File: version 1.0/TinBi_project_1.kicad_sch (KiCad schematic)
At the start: 57 parts

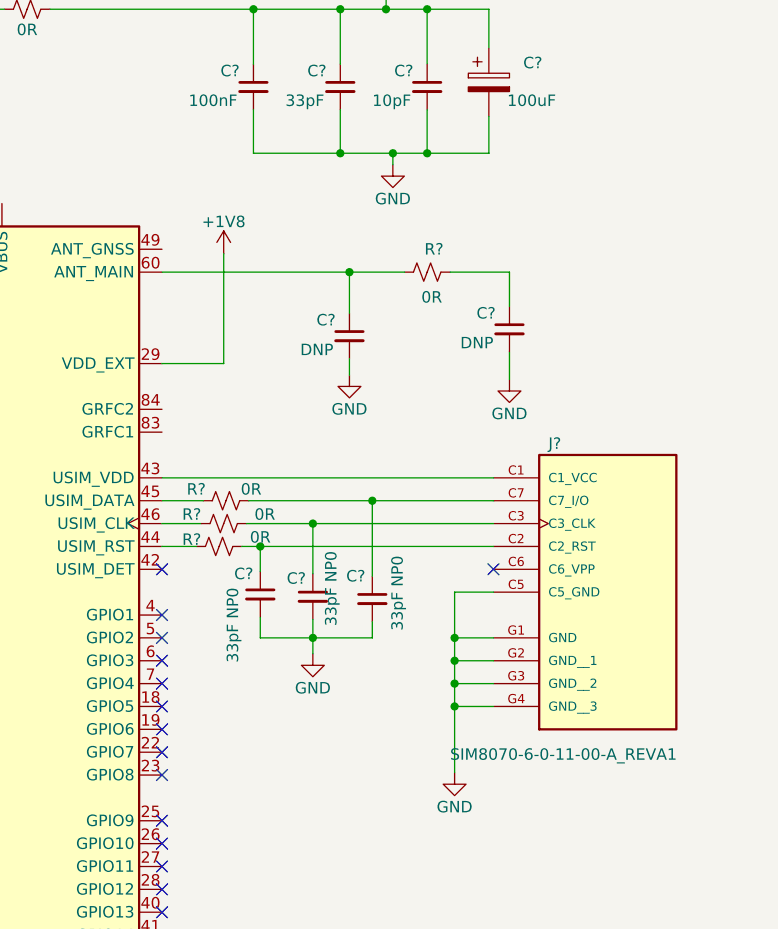
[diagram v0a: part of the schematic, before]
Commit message: Updated with the antenna symbols and library
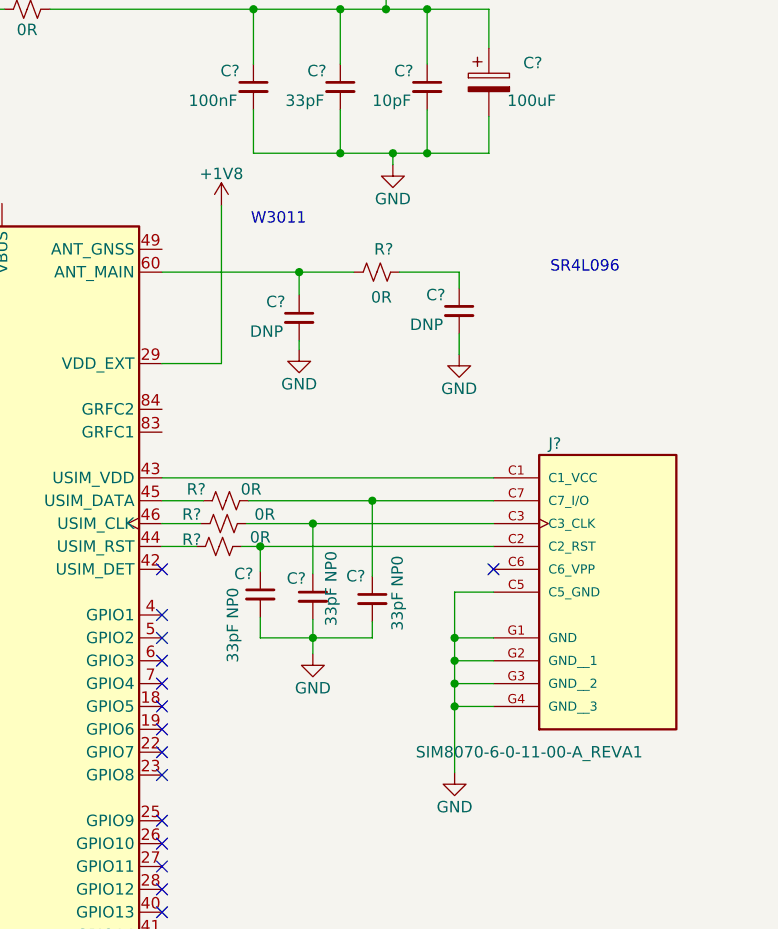
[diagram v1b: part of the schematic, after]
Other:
- note added: "SR4L096"
- note added: "W3011"
- moved on the sheet: C?, R?
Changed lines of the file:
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@@
 		)
 	)
+	(text "SR4L096 "
+		(exclude_from_sim no)
+		(at 371.094 61.976 0)
+		(effects
+			(font
+				(size 1.27 1.27)
+			)
+		)
+	)
 	(text "RESET CIRCUITRY"
 		(exclude_from_sim no)
@@
 		)
 	)
+	(text "W3011 "
+		(exclude_from_sim no)
+		(at 337.058 56.642 0)
+		(effects
+			(font
+				(size 1.27 1.27)
+			)
+		)
+	)
 	(text "Place close as possible \nto the individual VDD pins"
 		(exclude_from_sim no)
@@
 	)
 	(junction
-		(at 344.932 62.484)
+		(at 339.344 62.484)
 		(diameter 0)
 		(color 0 0 0 0)
@@
 	(wire
 		(pts
-			(xy 351.028 62.484) (xy 344.932 62.484)
+			(xy 345.44 62.484) (xy 339.344 62.484)
 		)
 		(stroke
@@
 	(wire
 		(pts
-			(xy 330.962 60.452) (xy 330.962 72.644)
+			(xy 330.708 55.118) (xy 330.708 72.644)
 		)
 		(stroke
@@
 	(wire
 		(pts
-			(xy 356.108 62.484) (xy 362.712 62.484)
+			(xy 350.52 62.484) (xy 357.124 62.484)
 		)
 		(stroke
@@
 	(wire
 		(pts
-			(xy 344.932 62.484) (xy 344.932 67.056)
+			(xy 339.344 62.484) (xy 339.344 65.024)
 		)
 		(stroke
@@
 	(wire
 		(pts
-			(xy 344.932 73.914) (xy 344.932 72.136)
+			(xy 339.344 71.12) (xy 339.344 70.104)
 		)
 		(stroke
@@
 	(wire
 		(pts
-			(xy 324.104 62.484) (xy 344.932 62.484)
+			(xy 324.104 62.484) (xy 339.344 62.484)
 		)
 		(stroke
@@
 	(wire
 		(pts
-			(xy 362.712 74.422) (xy 362.712 71.374)
+			(xy 357.124 71.628) (xy 357.124 69.342)
 		)
 		(stroke
@@
 	(wire
 		(pts
-			(xy 362.712 62.484) (xy 362.712 66.294)
+			(xy 357.124 62.484) (xy 357.124 64.262)
 		)
 		(stroke
@@
 	(wire
 		(pts
-			(xy 324.104 72.644) (xy 330.962 72.644)
+			(xy 324.104 72.644) (xy 330.708 72.644)
 		)
 		(stroke
@@
 		)
 		(property "Value" "SIM8070-6-0-11-00-A_REVA1"
-			(at 356.108 116.078 0)
+			(at 352.298 115.824 0)
 			(effects
 				(font
@@
 	(symbol
 		(lib_id "PCM_SparkFun-PowerSymbol:GND")
-		(at 362.712 74.422 0)
+		(at 357.124 71.628 0)
 		(unit 1)
 		(exclude_from_sim no)
@@
 		(fields_autoplaced yes)
 		(property "Reference" "#PWR042"
-			(at 362.712 80.772 0)
+			(at 357.124 77.978 0)
 			(effects
 				(font
@@
 		)
 		(property "Value" "GND"
-			(at 362.712 78.232 0)
+			(at 357.124 75.438 0)
 			(do_not_autoplace yes)
 			(effects
@@
 		)
 		(property "Footprint" ""
-			(at 362.712 74.422 0)
+			(at 357.124 71.628 0)
 			(effects
 				(font
@@
 		)
 		(property "Datasheet" ""
-			(at 362.712 74.422 0)
+			(at 357.124 71.628 0)
 			(effects
 				(font
@@
 		)
 		(property "Description" "Power symbol creates a global label with name \"GND\" , ground"
-			(at 362.712 83.312 0)
+			(at 357.124 80.518 0)
 			(effects
 				(font
@@
 	(symbol
 		(lib_id "power:+3V3")
-		(at 330.962 60.452 0)
+		(at 330.708 55.118 0)
 		(unit 1)
 		(exclude_from_sim no)
@@
 		(dnp no)
 		(property "Reference" "#PWR031"
-			(at 330.962 64.262 0)
+			(at 330.708 58.928 0)
 			(effects
 				(font
@@
 		)
 		(property "Value" "+1V8"
-			(at 330.962 56.896 0)
+			(at 330.708 51.562 0)
 			(effects
 				(font
@@
 		)
 		(property "Footprint" ""
-			(at 330.962 60.452 0)
+			(at 330.708 55.118 0)
 			(effects
 				(font
@@
 		)
 		(property "Datasheet" ""
-			(at 330.962 60.452 0)
+			(at 330.708 55.118 0)
 			(effects
 				(font
@@
 		)
 		(property "Description" "Power symbol creates a global label with name \"+3V3\""
-			(at 330.962 60.452 0)
+			(at 330.708 55.118 0)
 			(effects
 				(font
@@
 	(symbol
 		(lib_id "PCM_SparkFun-PowerSymbol:GND")
-		(at 344.932 73.914 0)
+		(at 339.344 71.12 0)
 		(unit 1)
 		(exclude_from_sim no)
@@
 		(fields_autoplaced yes)
 		(property "Reference" "#PWR041"
-			(at 344.932 80.264 0)
+			(at 339.344 77.47 0)
 			(effects
 				(font
@@
 		)
 		(property "Value" "GND"
-			(at 344.932 77.724 0)
+			(at 339.344 74.93 0)
 			(do_not_autoplace yes)
 			(effects
@@
 		)
 		(property "Footprint" ""
-			(at 344.932 73.914 0)
+			(at 339.344 71.12 0)
 			(effects
 				(font
@@
 		)
 		(property "Datasheet" ""
-			(at 344.932 73.914 0)
+			(at 339.344 71.12 0)
 			(effects
 				(font
@@
 		)
 		(property "Description" "Power symbol creates a global label with name \"GND\" , ground"
-			(at 344.932 82.804 0)
+			(at 339.344 80.01 0)
 			(effects
 				(font
@@
 	(symbol
 		(lib_id "Device:C_Small")
-		(at 344.932 69.596 0)
+		(at 339.344 67.564 0)
 		(unit 1)
 		(exclude_from_sim no)
@@
 		(dnp no)
 		(property "Reference" "C?"
-			(at 343.408 67.818 0)
+			(at 337.82 65.786 0)
 			(effects
 				(font
@@
 		)
 		(property "Value" "DNP"
-			(at 343.154 71.12 0)
+			(at 337.566 69.088 0)
 			(effects
 				(font
@@
 		)
 		(property "Footprint" ""
-			(at 344.932 69.596 0)
+			(at 339.344 67.564 0)
 			(effects
 				(font
@@
 		)
 		(property "Datasheet" "~"
-			(at 344.932 69.596 0)
+			(at 339.344 67.564 0)
 			(effects
 				(font
@@
 		)
 		(property "Description" "Unpolarized capacitor, small symbol"
-			(at 344.932 69.596 0)
+			(at 339.344 67.564 0)
 			(effects
 				(font
@@
 	(symbol
 		(lib_id "Device:C_Small")
-		(at 362.712 68.834 0)
+		(at 357.124 66.802 0)
 		(unit 1)
 		(exclude_from_sim no)
@@
 		(dnp no)
 		(property "Reference" "C?"
-			(at 361.188 67.056 0)
+			(at 355.6 65.024 0)
 			(effects
 				(font
@@
 		)
 		(property "Value" "DNP"
-			(at 360.934 70.358 0)
+			(at 355.346 68.326 0)
 			(effects
 				(font
@@
 		)
 		(property "Footprint" ""
-			(at 362.712 68.834 0)
+			(at 357.124 66.802 0)
 			(effects
 				(font
@@
 		)
 		(property "Datasheet" "~"
-			(at 362.712 68.834 0)
+			(at 357.124 66.802 0)
 			(effects
 				(font
@@
 		)
 		(property "Description" "Unpolarized capacitor, small symbol"
-			(at 362.712 68.834 0)
+			(at 357.124 66.802 0)
 			(effects
 				(font
@@
 	(symbol
 		(lib_id "PCM_SparkFun-Resistor:R_Small")
-		(at 353.568 62.484 180)
+		(at 347.98 62.484 180)
 		(unit 1)
 		(exclude_from_sim no)
@@
 		(dnp no)
 		(property "Reference" "R?"
-			(at 354.33 59.944 0)
+			(at 348.742 59.944 0)
 			(effects
 				(font
@@
 		)
 		(property "Value" "0R"
-			(at 354.076 65.278 0)
+			(at 348.488 65.278 0)
 			(effects
 				(font
@@
 		)
 		(property "Footprint" "PCM_SparkFun-Resistor:R_0603_1608Metric"
-			(at 353.568 57.912 0)
+			(at 347.98 57.912 0)
 			(effects
 				(font
@@
 		)
 		(property "Datasheet" "https://www.vishay.com/docs/20035/dcrcwe3.pdf"
-			(at 354.838 53.594 0)
+			(at 349.25 53.594 0)
 			(effects
 				(font
@@
 		)
 		(property "Description" "Resistor"
-			(at 353.568 51.054 0)
+			(at 347.98 51.054 0)
 			(effects
 				(font
@@
 		)
 		(property "PROD_ID" "RES-07856"
-			(at 353.568 55.626 0)
+			(at 347.98 55.626 0)
 			(effects
 				(font

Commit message: Todo; TVS SIM circuitry, trigger button, and boost circuitry
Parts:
- added AE?: W3011A, PCM_SparkFun-RF:GNSS_Ceramic_Antenna_18.0x18.0mm, symbol PCM_SparkFun-RF:Antenna_Ceramic_GNSS_18.0x18.0mm
- added ANT?: SR4L096, symbol TinBi_lib:SR4L096
- added C? (x2): 3pF NP0, symbol Device:C_Small
- added C?: 100nF, symbol Device:C_Small
- added D?: MMSD4148, Diode_SMD:D_SOD-123, symbol Diode:MMSD4148
- added D? (x2): APHHS1005LZGCK-V, PCM_SparkFun-LED:LED_0603_1608Metric, symbol PCM_SparkFun-LED:LED
- added J?: VC0720B015F, symbol Connector_Generic:Conn_01x02
- added L?: 6.8nH, symbol Device:L_Small
- added L?: 12nH, symbol Device:L_Small
- added Q? (x3): DMN3042L-7, symbol Transistor_FET:Q_NMOS_GSD
- added R? (x2): 100R, PCM_SparkFun-Resistor:R_0603_1608Metric, symbol PCM_SparkFun-Resistor:R_Small
- added R? (x5): 10k, PCM_SparkFun-Resistor:R_0603_1608Metric, symbol PCM_SparkFun-Resistor:R_Small
- added R?: 0R, PCM_SparkFun-Resistor:R_0603_1608Metric, symbol PCM_SparkFun-Resistor:R_Small
- added R? (x2): 750R, PCM_SparkFun-Resistor:R_0603_1608Metric, symbol PCM_SparkFun-Resistor:R_Small
- added U?: ~, symbol TinBi_lib:MX35LF4G24AD-Z4I
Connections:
- net +3V3: now also C?.2, D?.1 (K), D?.2 (A), D?.2 (A), J?.1 (Pin_1), R?.2, R?.2, U?.8 (VCC)
- net GND: now also AE?.2 (GND), C?.1, C?.2, L?.2, L?.2, Q?.2 (S), Q?.2 (S), Q?.2 (S), R?.1, R?.1, R?.1, U?.4 (GND)
- net at U?.20 (STATUS): now also R?.1
- net at U?.21 (NET_STATUS): now also R?.1
- net at U?.49 (ANT_GNSS): now also AE?.1 (A), C?.1
- net MEM_SIO3: now reaches U?.12 (PA6)
- net MEM_SIO3: now also U?.7 (~{HOLD}/SIO3)
- net MEM_SIO2: now reaches U?.13 (PA7)
- net MEM_SIO2: now also U?.3 (~{WP}/SIO2)
- net MEM_SIO1: now reaches U?.14 (PB0)
- net MEM_SIO1: now also U?.2 (SO/SIO1)
- net MEM_SIO0: now reaches U?.15 (PB1)
- net MEM_SIO0: now also U?.5 (SI/SIO0)
- net at U?.24 (PA14): now also Q?.3 (D), R?.1, R?.1
- net at U?.25 (PA15): now also Q?.3 (D), R?.1, R?.1
- net ~{MEM_CS}: now reaches U?.8 (PA2)
- net ~{MEM_CS}: now also U?.1 (~{CS})
- net MEM_SCLK: now reaches U?.9 (PA3)
- net MEM_SCLK: now also U?.6 (SCLK)
- net at C?.1, R?.1: now also R?.2
- new net: ANT?.5 (FEED), C?.1, L?.1
- new net: C?.2, L?.1, R?.1
- new net: Q?.1 (G), R?.2, R?.2 (x2)
- new net: D?.2 (A), J?.2 (Pin_2), Q?.3 (D)
- new net: D?.1 (K), R?.2 (x2)
- new net: ANT?.1 (NC), ANT?.10 (NC), ANT?.11 (NC), ANT?.12 (NC), ANT?.13 (NC), ANT?.14 (NC), ANT?.15 (NC), ANT?.16 (NC), ANT?.2 (NC), ANT?.3 (NC), ANT?.4 (NC), ANT?.6 (NC), ANT?.7 (NC), ANT?.8 (NC), ANT?.9 (NC)
- new net VIB_CNTRL: Q?.1 (G), R?.2
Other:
- note added: "ANTENNA CIRCUITRY"
- note added: "BACKUP-MEMORY"
- note added: "TODO; --> ANTENNA CIRCUITRY (done) --> SIM CIRCUTRY -> TPD4E110DPWR (ASSIGNMENT) --> STATUS LED (DONE) --> MEMORY CHIP CIRCUITRY (DONE) --> ACTUATOR; VIBRATION CIRCUITRY (DONE) --> TRIGGER BUTTON (ASSIGNMENT) --> STEP/BOOST CONVERTER CCT"
- note added: "VIBRATION MOTOR"
- note removed: "SR4L096"
- note removed: "TODO; --> ANTENNA CIRCUITRY --> SIM CIRCUTRY -> TVS --> STATUS LED --> MEMORY CHIP CIRCUITRY --> ACTUATOR; VIBRATION CIRCUITRY --> TRIGGER BUTTON --> STEP/BOOST CONVERTER CCT"
- note removed: "W3011"
- moved on the sheet: C?, R?, U?

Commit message: Updated designs
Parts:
- added BT1, BT2: CR2325, symbol Device:Battery_Cell
- added C3: 100nF, Capacitor_SMD:C_0402_1005Metric, symbol Device:C_Small
- added C32, C33: 10uF, symbol Device:C_Small
- added C34, C35, C37: 22uF, symbol Device:C_Small
- added C36: 0.1uF, Capacitor_SMD:C_0402_1005Metric, symbol Device:C_Small
- added JP1: Power Mode Selector, symbol Jumper:SolderJumper_3_Open
- added L3: 1.5uH, symbol Device:L_Small
- added R2, R28: 10k, PCM_SparkFun-Resistor:R_0603_1608Metric, symbol PCM_SparkFun-Resistor:R_Small
- added SW3: SW_Push, symbol Switch:SW_Push
- added U5: TPS63021DSJT, DSJ14_2P85X1P58, symbol TPS63021DSJT:TPS63021DSJT
- C1, C10, C11, C12, C14, C15, C16, C17, C18, C19, C2, C20, C22, C23, C25, C26, C28, C29, C30, C31, C4, C5, C7, C8, C9: renamed from C?; footprint (none) -> Capacitor_SMD:C_0402_1005Metric
- gave numbers to parts that had none: 57
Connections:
- net +3V3: now also C34.1, C35.1, C37.1, R2.2, U5.3 (FB), U5.4 (VOUT), U5.5 (VOUT)
- net GND: now also BT1.2 (-), BT2.2 (-), C3.2, C32.2, C33.2, C34.2, C35.2, C36.2, C37.2, JP1.1 (A), SW3.1, U5.15 (EPAD), U5.2 (GND)
- net GSM_TX: no longer Q6.2 (S), R19.1, U3.39 (MAIN_RI)
- net PS_CTRL: now reaches U2.18 (PA8)
- net PS_CTRL: now also JP1.2 (C), U5.13 (PS/SYNC)
- net PWR_GOOD: now reaches U2.22 (PA12)
- net PWR_GOOD: now also R28.1, U5.14 (PG)
- new net: C36.1, U5.1 (VINA), U5.12 (EN)
- new net: L3.2, U5.6 (L2), U5.7 (L2)
- new net: L3.1, U5.8 (L1), U5.9 (L1)
- new net +VBAT: BT1.1 (+), BT2.1 (+), C32.1, C33.1, JP1.3 (B), R28.2, U5.10 (VIN), U5.11 (VIN)
- new net GSM_RI: Q6.2 (S), R19.1, U3.39 (MAIN_RI)
- new net ~{TRIG_BUTTON}: C3.1, R2.1, SW3.2
- no-connect marks 35 -> 44
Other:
- note added: "EMERGENCY BUTTON"
- note added: "MAIN CIRCUITRY"
- note added: "POWER CIRCUITRY"
- note added: "Vmin-3.0 to 3.3V"
- moved on the sheet: D3, Q3, R13, R9

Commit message: Layout progress
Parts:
- removed R22, R23: 0R, PCM_SparkFun-Resistor:R_0603_1608Metric, symbol PCM_SparkFun-Resistor:R_Small
- added J3: PROJ/DEBUG, Connector_PinHeader_2.54mm:PinHeader_1x03_P2.54mm_Vertical, symbol Connector_Generic:Conn_01x03
- AE1: footprint PCM_SparkFun-RF:GNSS_Ceramic_Antenna_18.0x18.0mm -> RF_Antenna:Pulse_W3011
- ANT1: footprint (none) -> TinBi_FP:SR4L09
- BT1, BT2: footprint (none) -> Battery:BatteryHolder_ComfortableElectronic_CH273-2450_1x2450
- C13, C24, C27: footprint (none) -> Capacitor_SMD:C_0402_1005Metric
- C21: footprint (none) -> Capacitor_Tantalum_SMD:CP_EIA-7343-15_Kemet-W; MPN (none) -> T491W107K010AT
- C31: footprint Capacitor_SMD:C_0402_1005Metric -> Capacitor_SMD:C_0603_1608Metric
- C32, C33: footprint (none) -> Capacitor_SMD:C_0805_2012Metric; MPN (none) -> CL21B106KAYQNNE
- C34, C35, C37: footprint (none) -> Capacitor_SMD:C_0805_2012Metric; MPN (none) -> GRM21BZ71A226ME15L
- C38: footprint (none) -> Capacitor_Tantalum_SMD:CP_EIA-7343-15_Kemet-W
- C6: footprint (none) -> Capacitor_SMD:C_0805_2012Metric
- J1: footprint (none) -> hgo_lib_pl:3mm by 3mm pad
- J2: footprint SIM8070-6-0-11-00-A_REVA1:GCT_SIM8070-6-0-11-00-A_REVA1 -> SIM8070_6_0_11_00_A:GCT_SIM8070-6-0-11-00-A_REVA1
- JP1: footprint (none) -> Jumper:SolderJumper-3_P1.3mm_Open_RoundedPad1.0x1.5mm
- L1: footprint (none) -> Inductor_SMD:L_0402_1005Metric; MPN (none) -> AIMC-0402HQ-12NG-T
- L2: footprint (none) -> Inductor_SMD:L_0402_1005Metric; MPN (none) -> ASCH001005056N8JCP
- L3: footprint (none) -> Inductor_SMD:L_Coilcraft_XAL4020-XXX; MPN (none) -> XFL4020-152MEC
- Q1, Q2, Q3, Q4, Q5, Q6, Q7: footprint (none) -> Package_TO_SOT_SMD:SOT-23
- SW1, SW2, SW3: value SW_Push -> KMR211NG LFS; footprint (none) -> Button_Switch_SMD:SW_Push_1P1T_NO_CK_KMR2
- U1: value ~ -> MX35LF4G24AD; footprint (none) -> Package_SON:WSON-8-1EP_8x6mm_P1.27mm_EP3.4x4.3mm
- U5: footprint DSJ14_2P85X1P58 -> TPS63020DSJT:IC_TPS63020DSJT
- Y1: footprint PCM_SparkFun-Clock:Crystal-SMD-5x3.2mm -> ABM2_25_000MHZ_D4Y_T:XTAL_ABM2-25.000MHZ-D4Y-T
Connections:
- net +3V3: now also U3.32 (VBAT_BB), U3.33 (VBAT_BB), U3.52 (VBAT_RF), U3.53 (VBAT_RF)
- net GND: now also U1.9 (EP), J3.2 (Pin_2)
- net GSM_ANTD: now reaches ANT1.5 (FEED), C31.1, L2.1
- net GSM_ANTC: now reaches C31.2, L1.1, R29.1
- net at Q2.3 (D), R7.1, R8.1: now also U2.30 (PB7); no longer U2.24 (PA14)
- net GNSS_ANT: now reaches AE1.1 (A), C30.1, U3.49 (ANT_GNSS)
- net GSM_ANTA: now reaches C24.1, R27.2, U3.60 (ANT_MAIN)
- net SWDIO: now reaches U2.23 (PA13)
- net SWDIO: now also J3.1 (Pin_1)
- net GSM_ANTB: now reaches C27.1, R27.1, R29.2
- new net SWDCLK: J3.3 (Pin_3), U2.24 (PA14)
- no-connect marks 44 -> 42
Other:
- note added: "ACTUATOR"
- note added: "ANT1"
- note added: "ANT2"
- note added: "BTN"
- note added: "GSM"
- note added: "MCU"
- note added: "MEM"
- note added: "MIC1"
- note added: "MIC2"
- note added: "PWR CCT"
- note added: "T491W107K010AT"
- moved on the sheet: C31
